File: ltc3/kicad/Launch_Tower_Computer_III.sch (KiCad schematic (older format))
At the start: 0 parts

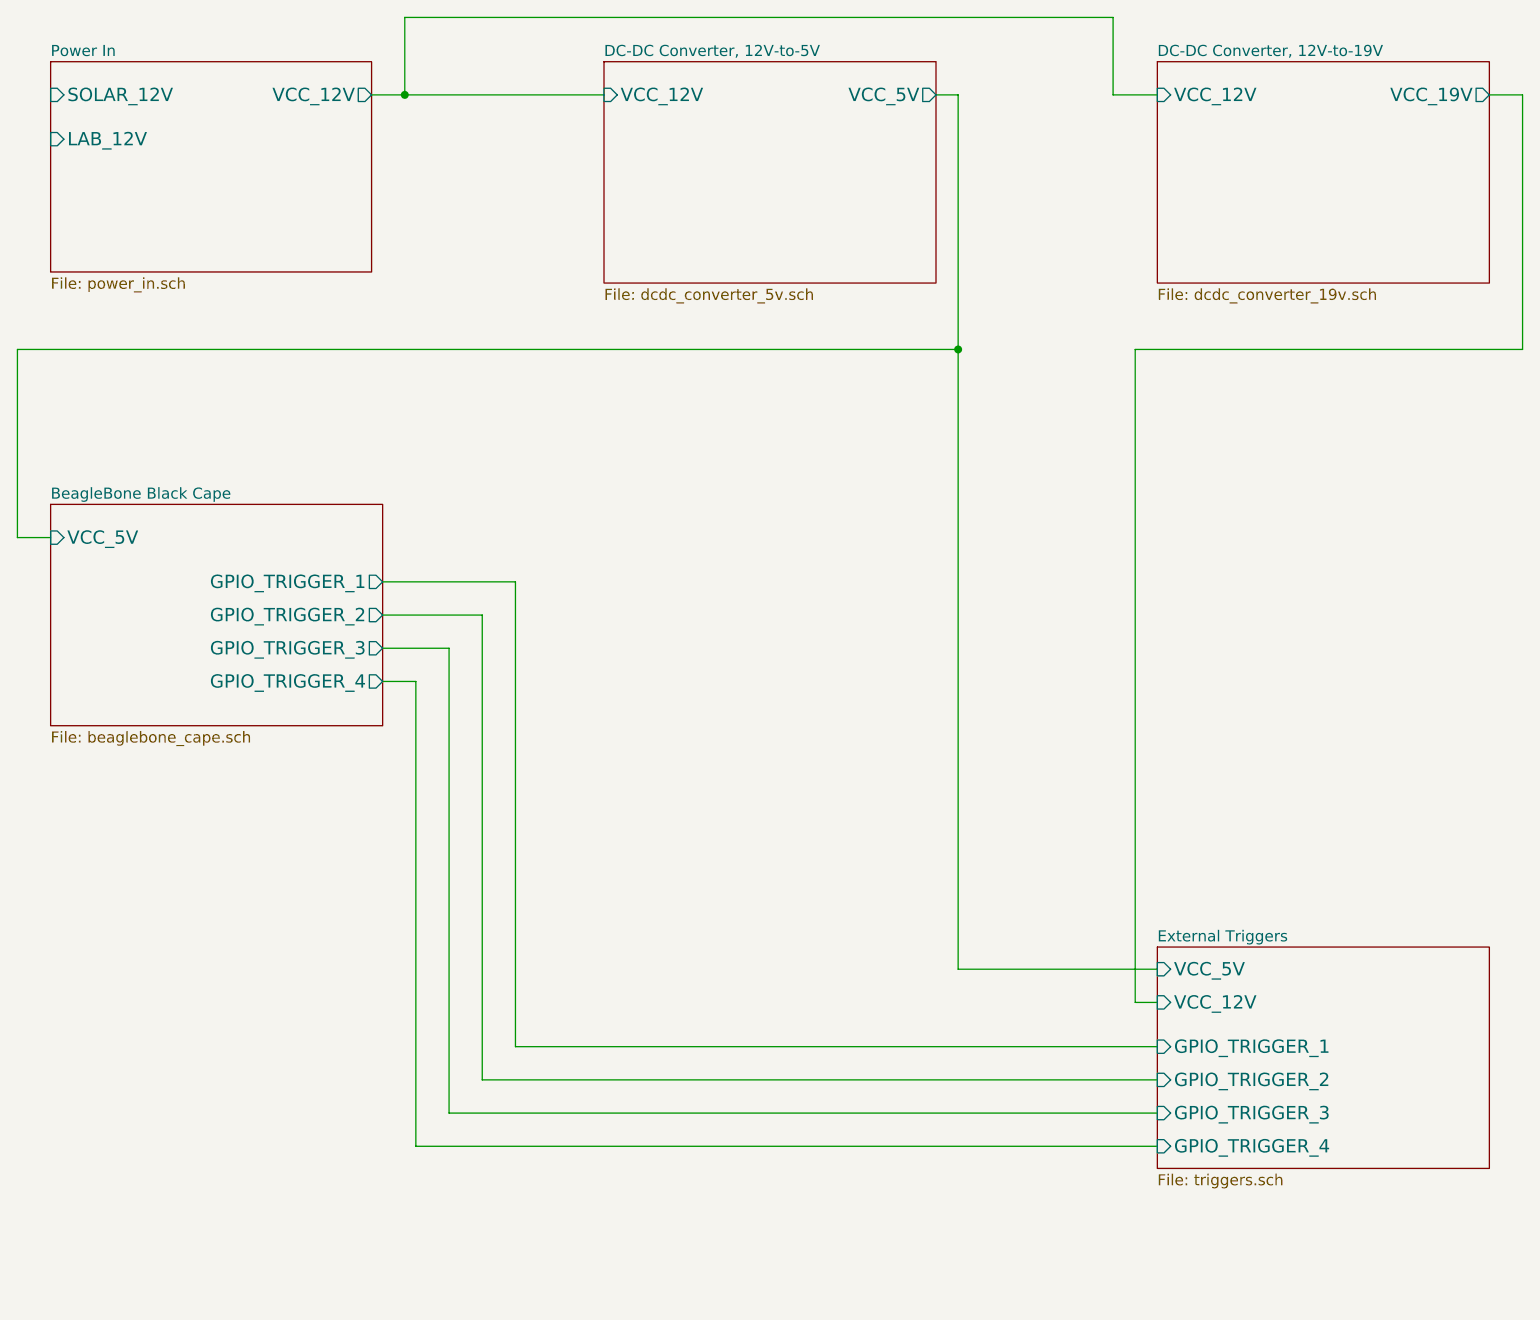
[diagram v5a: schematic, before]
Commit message: More progress on LTC3 schematic. Finished first draft of external device support (power and triggers). Added a few new datasheets.
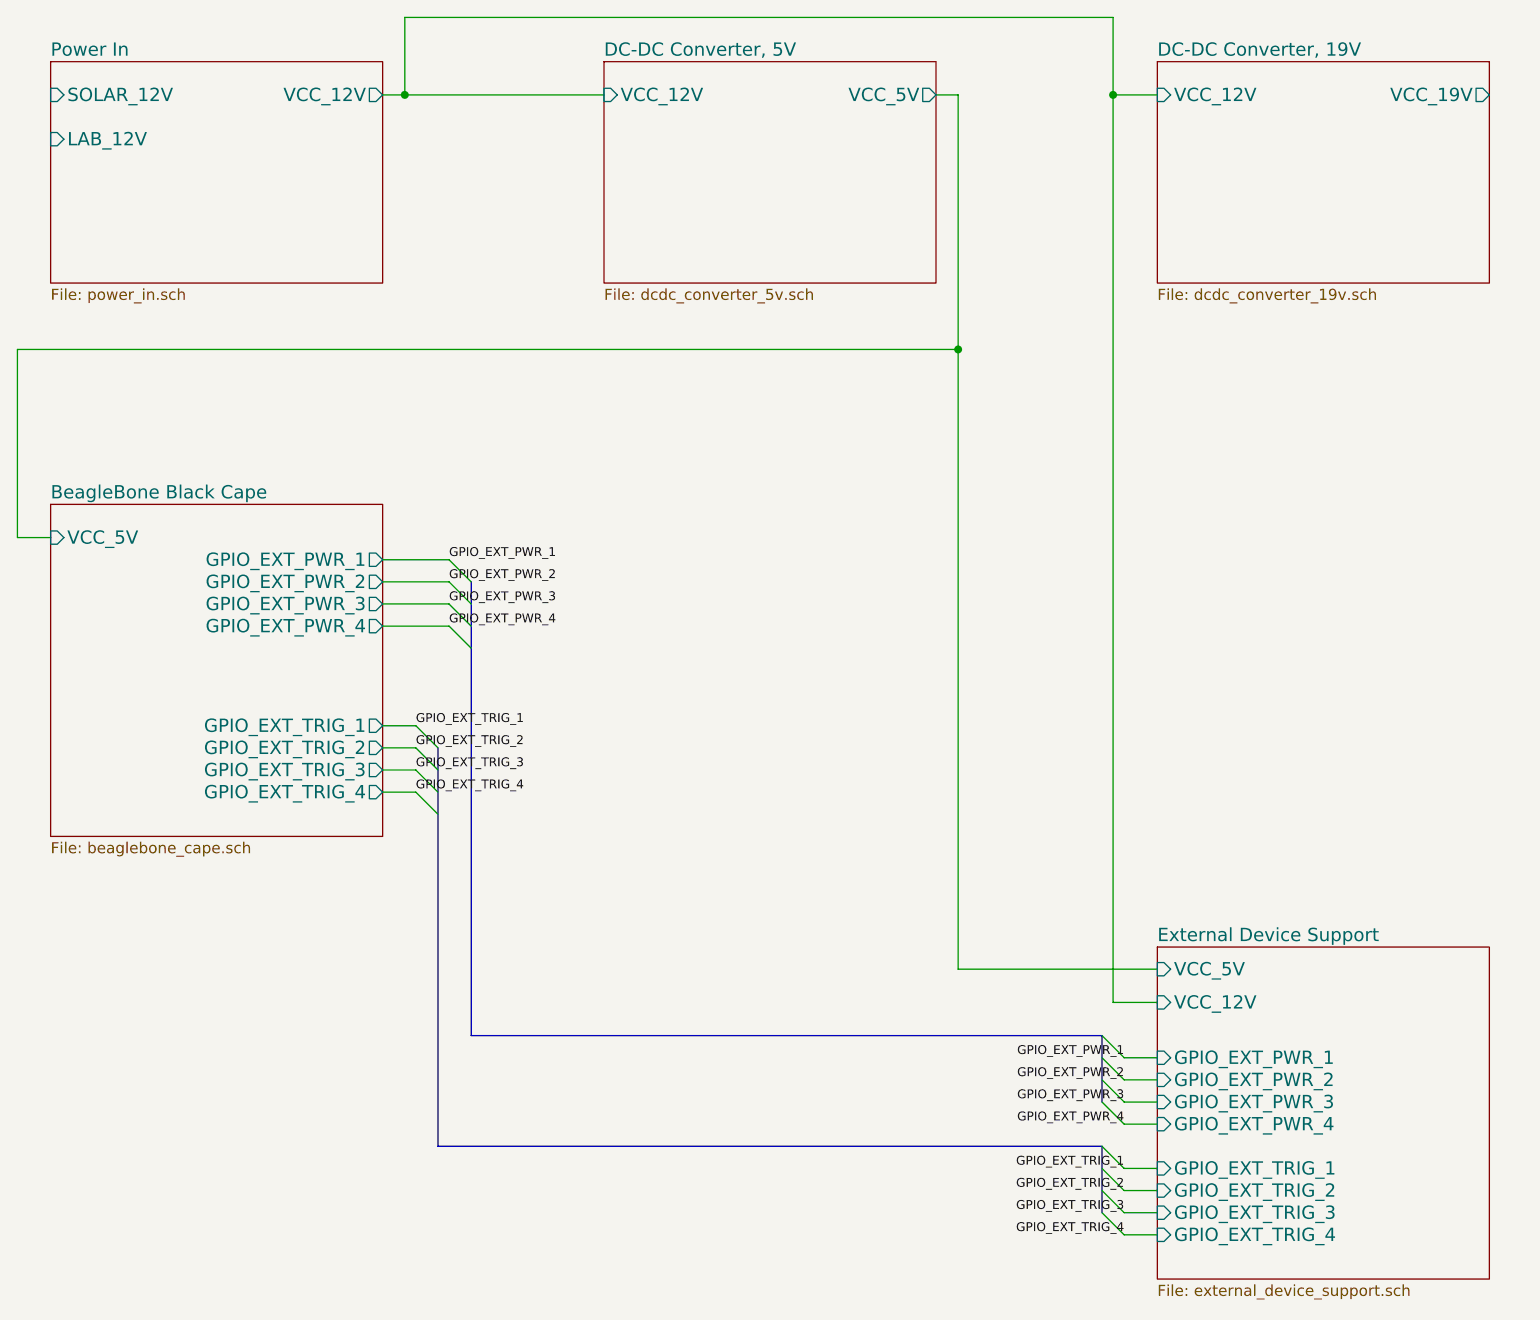
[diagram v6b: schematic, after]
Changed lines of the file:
@@
 LIBS:memory_devices
 LIBS:switches
+LIBS:Toshiba
 LIBS:Launch_Tower_Computer_III-cache
 EELAYER 27 0
 EELAYER END
-$Descr USLetter 11000 8500
+$Descr B 17000 11000
 encoding utf-8
 Sheet 1 6
 Title "Launch Tower Computer III (LTC3)"
-Date "4 apr 2015"
+Date "8 apr 2015"
 Rev "1"
 Comp "Portland State Aerospace Society <http://psas.pdx.edu/>"
@@
 $EndDescr
 $Sheet
-S 1000 1100 1450 950
+S 1000 1100 1500 1000
 U 551C8EE6
-F0 "Power In" 50
+F0 "Power In" 60
 F1 "power_in.sch" 50
-F2 "VCC_12V" O R 2450 1250 60
+F2 "VCC_12V" O R 2500 1250 60
 F3 "SOLAR_12V" I L 1000 1250 60
 F4 "LAB_12V" I L 1000 1450 60
@@
 S 3500 1100 1500 1000
 U 550535FB
-F0 "DC-DC Converter, 12V-to-5V" 50
+F0 "DC-DC Converter, 5V" 60
 F1 "dcdc_converter_5v.sch" 50
 F2 "VCC_5V" O R 5000 1250 60
@@
 S 6000 1100 1500 1000
 U 55053600
-F0 "DC-DC Converter, 12V-to-19V" 50
+F0 "DC-DC Converter, 19V" 60
 F1 "dcdc_converter_19v.sch" 50
 F2 "VCC_19V" O R 7500 1250 60
 F3 "VCC_12V" I L 6000 1250 60
 $EndSheet
-$Sheet
-S 1000 3100 1500 1000
+Wire Wire Line
+	2600 1250 2600 900
+Wire Wire Line
+	2600 900  5800 900
+Wire Wire Line
+	5800 900  5800 5350
+Wire Wire Line
+	5800 1250 6000 1250
+Connection ~ 2600 1250
+Wire Wire Line
+	5000 1250 5100 1250
+Wire Wire Line
+	5100 1250 5100 5200
+Wire Wire Line
+	5100 2400 850  2400
+Wire Wire Line
+	850  2400 850  3250
+Wire Wire Line
+	850  3250 1000 3250
+Wire Wire Line
+	5100 5200 6000 5200
+Connection ~ 5100 2400
+Wire Wire Line
+	2500 1250 3500 1250
+$Sheet
+S 1000 3100 1500 1500
 U 55051BA8
-F0 "BeagleBone Black Cape" 50
+F0 "BeagleBone Black Cape" 60
 F1 "beaglebone_cape.sch" 50
 F2 "VCC_5V" I L 1000 3250 60
-F3 "GPIO_TRIGGER_1" O R 2500 3450 60
-F4 "GPIO_TRIGGER_2" O R 2500 3600 60
-F5 "GPIO_TRIGGER_3" O R 2500 3750 60
-F6 "GPIO_TRIGGER_4" O R 2500 3900 60
-$EndSheet
-$Sheet
-S 6000 5100 1500 1000
+F3 "GPIO_EXT_TRIG_1" O R 2500 4100 60
+F4 "GPIO_EXT_TRIG_2" O R 2500 4200 60
+F5 "GPIO_EXT_TRIG_3" O R 2500 4300 60
+F6 "GPIO_EXT_TRIG_4" O R 2500 4400 60
+F7 "GPIO_EXT_PWR_1" O R 2500 3350 60
+F8 "GPIO_EXT_PWR_2" O R 2500 3450 60
+F9 "GPIO_EXT_PWR_3" O R 2500 3550 60
+F10 "GPIO_EXT_PWR_4" O R 2500 3650 60
+$EndSheet
+$Sheet
+S 6000 5100 1500 1500
 U 551C79BE
-F0 "External Triggers" 50
-F1 "triggers.sch" 50
-F2 "GPIO_TRIGGER_1" I L 6000 5550 60
-F3 "GPIO_TRIGGER_2" I L 6000 5700 60
-F4 "GPIO_TRIGGER_3" I L 6000 5850 60
-F5 "GPIO_TRIGGER_4" I L 6000 6000 60
-F6 "VCC_12V" I L 6000 5350 60
-F7 "VCC_5V" I L 6000 5200 60
-$EndSheet
-Wire Wire Line
-	2450 1250 3500 1250
-Wire Wire Line
-	2600 1250 2600 900
-Wire Wire Line
-	2600 900  5800 900
-Wire Wire Line
-	5800 900  5800 1250
-Wire Wire Line
-	5800 1250 6000 1250
-Connection ~ 2600 1250
-Wire Wire Line
-	5000 1250 5100 1250
-Wire Wire Line
-	5100 1250 5100 5200
-Wire Wire Line
-	5100 2400 850  2400
-Wire Wire Line
-	850  2400 850  3250
-Wire Wire Line
-	850  3250 1000 3250
-Wire Wire Line
-	5100 5200 6000 5200
-Connection ~ 5100 2400
-Wire Wire Line
-	6000 5350 5900 5350
-Wire Wire Line
-	5900 5350 5900 2400
-Wire Wire Line
-	5900 2400 7650 2400
-Wire Wire Line
-	7650 2400 7650 1250
-Wire Wire Line
-	7650 1250 7500 1250
-Wire Wire Line
-	2500 3900 2650 3900
-Wire Wire Line
-	2650 3900 2650 6000
-Wire Wire Line
-	2650 6000 6000 6000
-Wire Wire Line
-	2500 3750 2800 3750
-Wire Wire Line
-	2800 3750 2800 5850
-Wire Wire Line
-	2800 5850 6000 5850
-Wire Wire Line
-	2500 3600 2950 3600
-Wire Wire Line
-	2950 3600 2950 5700
-Wire Wire Line
-	2950 5700 6000 5700
-Wire Wire Line
-	2500 3450 3100 3450
-Wire Wire Line
-	3100 3450 3100 5550
-Wire Wire Line
-	3100 5550 6000 5550
+F0 "External Device Support" 60
+F1 "external_device_support.sch" 50
+F2 "VCC_12V" I L 6000 5350 60
+F3 "VCC_5V" I L 6000 5200 60
+F4 "GPIO_EXT_TRIG_1" I L 6000 6100 60
+F5 "GPIO_EXT_TRIG_2" I L 6000 6200 60
+F6 "GPIO_EXT_TRIG_3" I L 6000 6300 60
+F7 "GPIO_EXT_TRIG_4" I L 6000 6400 60
+F8 "GPIO_EXT_PWR_1" I L 6000 5600 60
+F9 "GPIO_EXT_PWR_2" I L 6000 5700 60
+F10 "GPIO_EXT_PWR_4" I L 6000 5900 60
+F11 "GPIO_EXT_PWR_3" I L 6000 5800 60
+$EndSheet
+Wire Wire Line
+	2500 3350 2800 3350
+Wire Wire Line
+	2500 3450 2800 3450
+Wire Wire Line
+	2500 3550 2800 3550
+Wire Wire Line
+	2500 3650 2800 3650
+Wire Wire Line
+	2500 4100 2650 4100
+Wire Wire Line
+	2500 4200 2650 4200
+Wire Wire Line
+	2500 4300 2650 4300
+Wire Wire Line
+	2500 4400 2650 4400
+Entry Wire Line
+	2800 3350 2900 3450
+Entry Wire Line
+	2800 3450 2900 3550
+Entry Wire Line
+	2800 3550 2900 3650
+Entry Wire Line
+	2800 3650 2900 3750
+Entry Wire Line
+	2650 4100 2750 4200
+Entry Wire Line
+	2650 4200 2750 4300
+Entry Wire Line
+	2650 4300 2750 4400
+Entry Wire Line
+	2650 4400 2750 4500
+Wire Wire Line
+	6000 5600 5850 5600
+Wire Wire Line
+	6000 5700 5850 5700
+Wire Wire Line
+	6000 5800 5850 5800
+Wire Wire Line
+	6000 5900 5850 5900
+Wire Wire Line
+	6000 6100 5850 6100
+Wire Wire Line
+	6000 6200 5850 6200
+Wire Wire Line
+	6000 6300 5850 6300
+Wire Wire Line
+	6000 6400 5850 6400
+Entry Wire Line
+	5750 5500 5850 5600
+Entry Wire Line
+	5750 5600 5850 5700
+Entry Wire Line
+	5750 5700 5850 5800
+Entry Wire Line
+	5750 5800 5850 5900
+Entry Wire Line
+	5750 6000 5850 6100
+Entry Wire Line
+	5750 6100 5850 6200
+Entry Wire Line
+	5750 6200 5850 6300
+Entry Wire Line
+	5750 6300 5850 6400
+Wire Bus Line
+	2750 4200 2750 6000
+Wire Bus Line
+	2750 6000 5750 6000
+Wire Bus Line
+	5750 6000 5750 6300
+Wire Bus Line
+	2900 3450 2900 5500
+Wire Bus Line
+	2900 5500 5750 5500
+Wire Bus Line
+	5750 5500 5750 5800
+Text Label 2800 3350 0    40   ~ 0
+GPIO_EXT_PWR_1
+Text Label 2800 3450 0    40   ~ 0
+GPIO_EXT_PWR_2
+Text Label 2800 3550 0    40   ~ 0
+GPIO_EXT_PWR_3
+Text Label 2800 3650 0    40   ~ 0
+GPIO_EXT_PWR_4
+Text Label 2650 4100 0    40   ~ 0
+GPIO_EXT_TRIG_1
+Text Label 2650 4200 0    40   ~ 0
+GPIO_EXT_TRIG_2
+Text Label 2650 4300 0    40   ~ 0
+GPIO_EXT_TRIG_3
+Text Label 2650 4400 0    40   ~ 0
+GPIO_EXT_TRIG_4
+Text Label 5850 5600 2    40   ~ 0
+GPIO_EXT_PWR_1
+Text Label 5850 5700 2    40   ~ 0
+GPIO_EXT_PWR_2
+Text Label 5850 5800 2    40   ~ 0
+GPIO_EXT_PWR_3
+Text Label 5850 5900 2    40   ~ 0
+GPIO_EXT_PWR_4
+Text Label 5850 6100 2    40   ~ 0
+GPIO_EXT_TRIG_1
+Text Label 5850 6200 2    40   ~ 0
+GPIO_EXT_TRIG_2
+Text Label 5850 6300 2    40   ~ 0
+GPIO_EXT_TRIG_3
+Text Label 5850 6400 2    40   ~ 0
+GPIO_EXT_TRIG_4
+Wire Wire Line
+	5800 5350 6000 5350
+Connection ~ 5800 1250
 $EndSCHEMATC
